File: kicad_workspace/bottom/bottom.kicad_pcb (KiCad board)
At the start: 4 copper layers, 76.8 x 84 mm, 76 parts, among them J1 691103110002, J2 BackupPad, J4 RPI_POWER_CONN, J5 UART_HEADER, J6 BackupPad, J7 Conn_01x05_Pin, M1 N20_MOTOR_EXTENDED_SHAFT, M2 N20_MOTOR_EXTENDED_SHAFT, U1 DRV8833PWP, U12 ACS712-5A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

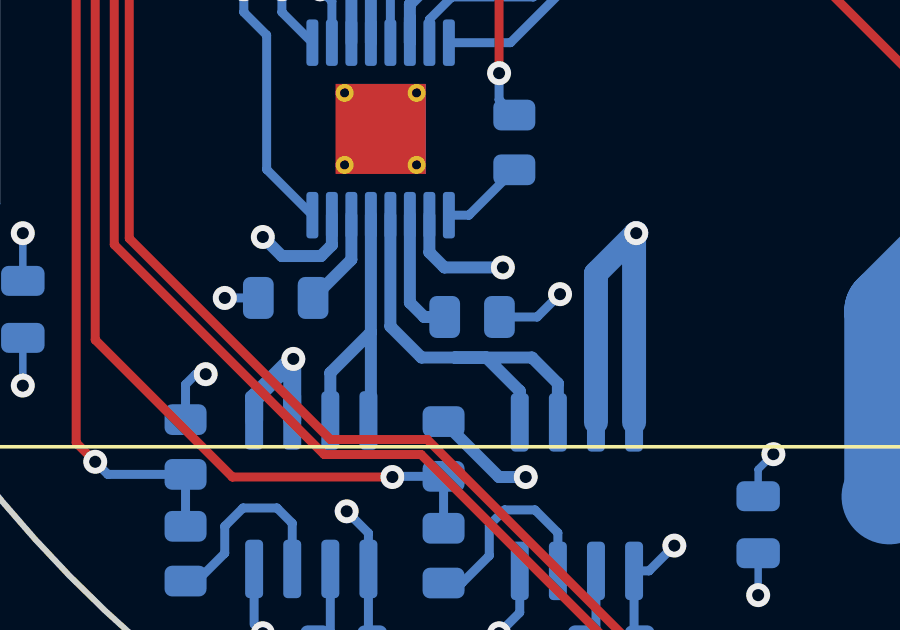
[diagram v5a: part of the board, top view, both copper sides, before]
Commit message: add additional vias for motor pins
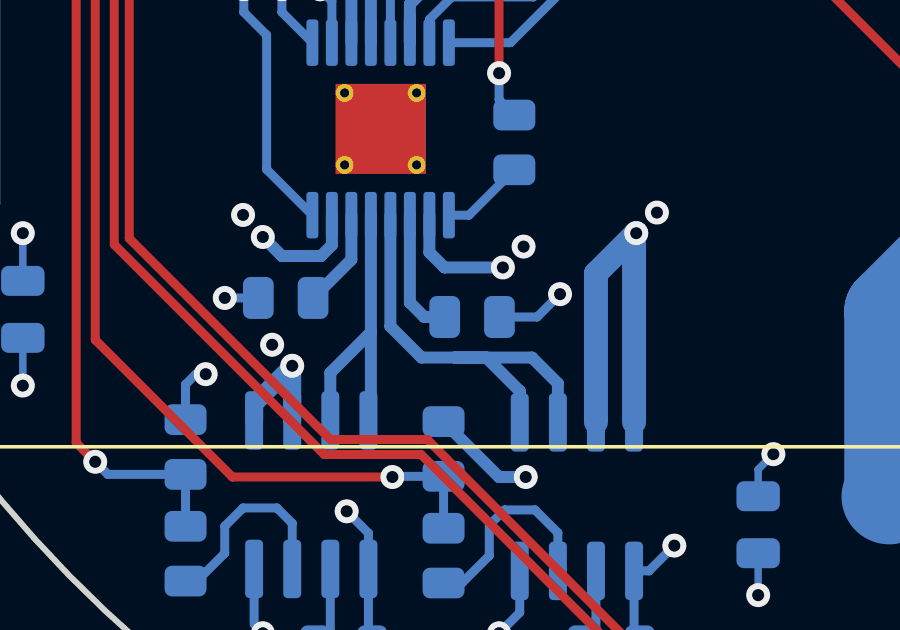
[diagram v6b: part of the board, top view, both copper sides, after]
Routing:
- net /MOTOR_B-: track 53.5 -> 55.6 mm, vias 2 -> 3
- net IP_MOTOR_B+: track 60.7 -> 62.7 mm, vias 2 -> 3
- net IP_MOTOR_A+: vias 2 -> 3
- net /MOTOR_A-: vias 2 -> 3
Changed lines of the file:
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@@
     (fp_arc (start -4.277996 -4.277996) (mid -5.350166 -3.264983) (end -6.75 -2.8)
       (stroke (width 0.12) (type solid)) (layer "B.SilkS"))
-    (fp_arc (start 4.277996 4.277996) (mid 5.350166 3.264983) (end 6.75 2.8)
+    (fp_arc (start 4.277996 4.277996) (mid 5.350166 3.264984) (end 6.75 2.8)
       (stroke (width 0.12) (type solid)) (layer "B.SilkS"))
     (fp_arc (start 5.988332 0.861605) (mid 0 6.049999) (end -5.988332 0.861605)
@@
   (segment (start 58.674 63.754) (end 58.674 65.532) (width 1) (layer "F.Cu") (net 5))
   (segment (start 55.8 63) (end 57.92 63) (width 1) (layer "F.Cu") (net 5))
+  (via (at 49.585355 77.290955) (size 0.8) (drill 0.4) (layers "F.Cu" "B.Cu") (net 5))
   (via (at 48.895 77.978) (size 0.8) (drill 0.4) (layers "F.Cu" "B.Cu") (net 5))
   (via (at 58.674 65.532) (size 0.8) (drill 0.4) (layers "F.Cu" "B.Cu") (net 5))
-  (segment (start 49.60175 77.270853) (end 50.886618 75.985985) (width 1.5) (layer "In2.Cu") (net 5))
+  (segment (start 50.886618 75.985985) (end 50.886618 73.319382) (width 1.5) (layer "In2.Cu") (net 5))
+  (segment (start 49.585355 77.287248) (end 50.886618 75.985985) (width 1.5) (layer "In2.Cu") (net 5))
   (segment (start 50.886618 73.319382) (end 58.674 65.532) (width 1.5) (layer "In2.Cu") (net 5))
+  (segment (start 49.585355 77.290955) (end 49.585355 77.287248) (width 1.5) (layer "In2.Cu") (net 5))
   (segment (start 49.515132 77.357868) (end 48.895 77.978) (width 1.5) (layer "In2.Cu") (net 5))
-  (segment (start 50.886618 75.985985) (end 50.886618 73.319382) (width 1.5) (layer "In2.Cu") (net 5))
   (segment (start 48.895 77.978) (end 48.895 77.926326) (width 0.8) (layer "In2.Cu") (net 5))
+  (segment (start 49.585355 77.287248) (end 49.60175 77.270853) (width 1.5) (layer "In2.Cu") (net 5))
   (segment (start 48.823 78.05) (end 48.895 77.978) (width 0.8) (layer "B.Cu") (net 5))
   (segment (start 47.553 79.32) (end 47.553 84.285) (width 0.8) (layer "B.Cu") (net 5))
@@
   (segment (start 55.8 65) (end 53.425875 65) (width 1) (layer "F.Cu") (net 97))
   (via (at 44.45 79.121) (size 0.8) (drill 0.4) (layers "F.Cu" "B.Cu") (net 97))
+  (via (at 45.140488 78.425612) (size 0.8) (drill 0.4) (layers "F.Cu" "B.Cu") (net 97))
   (via (at 53.408501 64.982626) (size 0.8) (drill 0.4) (layers "F.Cu" "B.Cu") (net 97))
-  (segment (start 44.45 79.121) (end 47.244 76.327) (width 1.5) (layer "In2.Cu") (net 97))
+  (segment (start 45.140488 78.425612) (end 45.140488 78.430512) (width 1.5) (layer "In2.Cu") (net 97))
   (segment (start 47.244 71.147127) (end 49.289564 69.101564) (width 1.5) (layer "In2.Cu") (net 97))
+  (segment (start 45.145388 78.425612) (end 47.244 76.327) (width 1.5) (layer "In2.Cu") (net 97))
+  (segment (start 47.244 76.327) (end 47.244 71.147127) (width 1.5) (layer "In2.Cu") (net 97))
+  (segment (start 45.140488 78.425612) (end 45.145388 78.425612) (width 1.5) (layer "In2.Cu") (net 97))
   (segment (start 49.289564 69.101564) (end 53.408501 64.982626) (width 1.5) (layer "In2.Cu") (net 97))
+  (segment (start 45.140488 78.430512) (end 44.45 79.121) (width 1.5) (layer "In2.Cu") (net 97))
   (segment (start 47.779128 70.612) (end 49.289564 69.101564) (width 1.5) (layer "In2.Cu") (net 97))
-  (segment (start 47.244 76.327) (end 47.244 71.147127) (width 1.5) (layer "In2.Cu") (net 97))
   (segment (start 42.5025 79.121) (end 42 78.6185) (width 0.4) (layer "B.Cu") (net 97))
   (segment (start 42 78.6185) (end 42 77.378) (width 0.4) (layer "B.Cu") (net 97))
@@
   (segment (start 66.294 58.674) (end 64.62 57) (width 1) (layer "F.Cu") (net 98))
   (segment (start 66.294 61.468) (end 66.294 58.674) (width 1) (layer "F.Cu") (net 98))
+  (via (at 35.789368 77.370148) (size 0.8) (drill 0.4) (layers "F.Cu" "B.Cu") (net 98))
   (via (at 66.548 61.722) (size 0.8) (drill 0.4) (layers "F.Cu" "B.Cu") (net 98))
   (via (at 36.449 78.105) (size 0.8) (drill 0.4) (layers "F.Cu" "B.Cu") (net 98))
+  (segment (start 35.714148 77.370148) (end 36.449 78.105) (width 1.5) (layer "In2.Cu") (net 98))
   (segment (start 50.135101 82.452899) (end 40.796899 82.452899) (width 1.5) (layer "In2.Cu") (net 98))
   (segment (start 66.548 61.722) (end 67.564 62.738) (width 1.5) (layer "In2.Cu") (net 98))
   (segment (start 67.564 65.024) (end 50.135101 82.452899) (width 1.5) (layer "In2.Cu") (net 98))
+  (segment (start 35.789368 77.370148) (end 35.714148 77.370148) (width 1.5) (layer "In2.Cu") (net 98))
+  (segment (start 35.789368 77.445368) (end 35.789368 77.370148) (width 1.5) (layer "In2.Cu") (net 98))
   (segment (start 67.564 62.738) (end 67.564 65.024) (width 1.5) (layer "In2.Cu") (net 98))
-  (segment (start 40.796899 82.452899) (end 36.449 78.105) (width 1.5) (layer "In2.Cu") (net 98))
+  (segment (start 40.796899 82.452899) (end 35.789368 77.445368) (width 1.5) (layer "In2.Cu") (net 98))
   (segment (start 38.75 78.3755) (end 38.3855 78.74) (width 0.4) (layer "B.Cu") (net 98))
   (segment (start 38.3855 78.74) (end 37.084 78.74) (width 0.4) (layer "B.Cu") (net 98))
@@
   (segment (start 64.2 55) (end 64.825056 55) (width 1) (layer "F.Cu") (net 102))
   (segment (start 68.453 58.801) (end 64.652 55) (width 1) (layer "F.Cu") (net 102))
-  (via (at 37.465 82.169) (size 0.8) (drill 0.4) (layers "F.Cu" "B.Cu") (net 102))
+  (via (at 37.428125 82.398765) (size 0.8) (drill 0.4) (layers "F.Cu" "B.Cu") (net 102))
   (via (at 68.453 58.801) (size 0.8) (drill 0.4) (layers "F.Cu" "B.Cu") (net 102))
-  (segment (start 39.20533 84.363798) (end 37.465 82.623468) (width 1.5) (layer "In2.Cu") (net 102))
-  (segment (start 70.612 65.278) (end 51.526202 84.363798) (width 1.5) (layer "In2.Cu") (net 102))
-  (segment (start 51.526202 84.363798) (end 39.20533 84.363798) (width 1.5) (layer "In2.Cu") (net 102))
-  (segment (start 37.465 82.623468) (end 37.465 82.169) (width 1.5) (layer "In2.Cu") (net 102))
-  (segment (start 68.453 58.801) (end 70.612 60.96) (width 1.5) (layer "In2.Cu") (net 102))
-  (segment (start 70.612 60.96) (end 70.612 65.278) (width 1.5) (layer "In2.Cu") (net 102))
-  (segment (start 36.158125 83.475875) (end 37.465 82.169) (width 0.6) (layer "B.Cu") (net 102))
-  (segment (start 37.428125 84.22) (end 37.428125 82.205875) (width 0.6) (layer "B.Cu") (net 102))
-  (segment (start 37.428125 82.205875) (end 37.465 82.169) (width 0.6) (layer "B.Cu") (net 102))
-  (segment (start 36.158125 84.22) (end 36.158125 83.475875) (width 0.6) (layer "B.Cu") (net 102))
+  (via (at 36.758752 81.696888) (size 0.8) (drill 0.4) (layers "F.Cu" "B.Cu") (net 102))
+  (segment (start 51.526202 84.363798) (end 70.612 65.278) (width 1.5) (layer "In2.Cu") (net 102))
+  (segment (start 36.758752 81.696888) (end 36.758752 81.91722) (width 1.5) (layer "In2.Cu") (net 102))
+  (segment (start 70.612 65.278) (end 70.612 60.96) (width 1.5) (layer "In2.Cu") (net 102))
+  (segment (start 36.660159 81.818627) (end 37.872766 83.031234) (width 1.5) (layer "In2.Cu") (net 102))
+  (segment (start 39.20533 84.363798) (end 51.526202 84.363798) (width 1.5) (layer "In2.Cu") (net 102))
+  (segment (start 37.872766 83.031234) (end 39.20533 84.363798) (width 1.5) (layer "In2.Cu") (net 102))
+  (segment (start 70.612 60.96) (end 68.453 58.801) (width 1.5) (layer "In2.Cu") (net 102))
+  (segment (start 36.758752 81.91722) (end 37.872766 83.031234) (width 1.5) (layer "In2.Cu") (net 102))
+  (segment (start 36.158125 83.668765) (end 36.158125 84.22) (width 0.6) (layer "B.Cu") (net 102))
+  (segment (start 37.428125 82.398765) (end 37.428125 84.22) (width 0.6) (layer "B.Cu") (net 102))
+  (segment (start 37.428125 82.398765) (end 36.158125 83.668765) (width 0.6) (layer "B.Cu") (net 102))
   (segment (start 42.65 77.378) (end 43.319 77.378) (width 0.3) (layer "B.Cu") (net 103))
   (segment (start 43.319 77.378) (end 44.831 75.866) (width 0.3) (layer "B.Cu") (net 103))

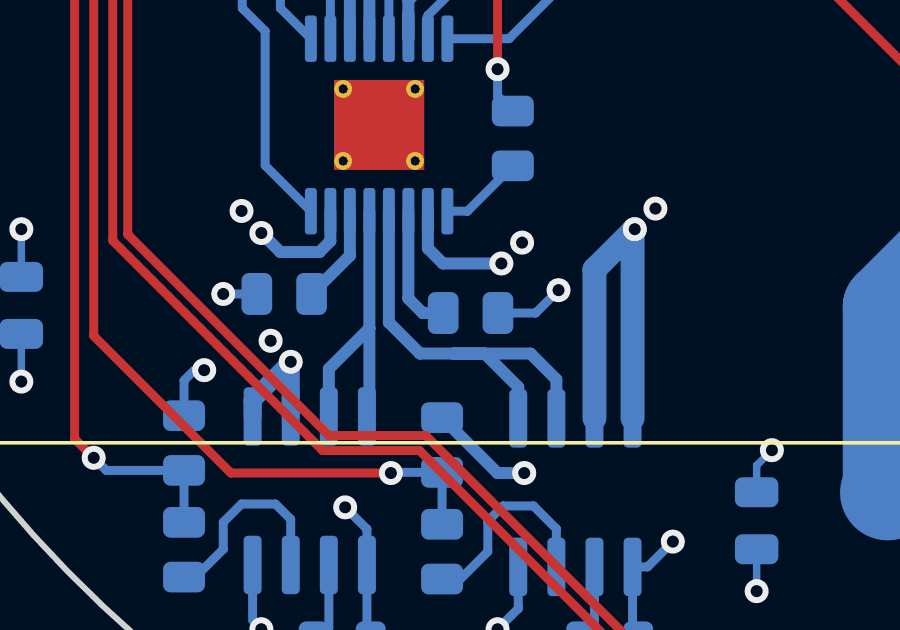
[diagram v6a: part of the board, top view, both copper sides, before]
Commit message: fix traces
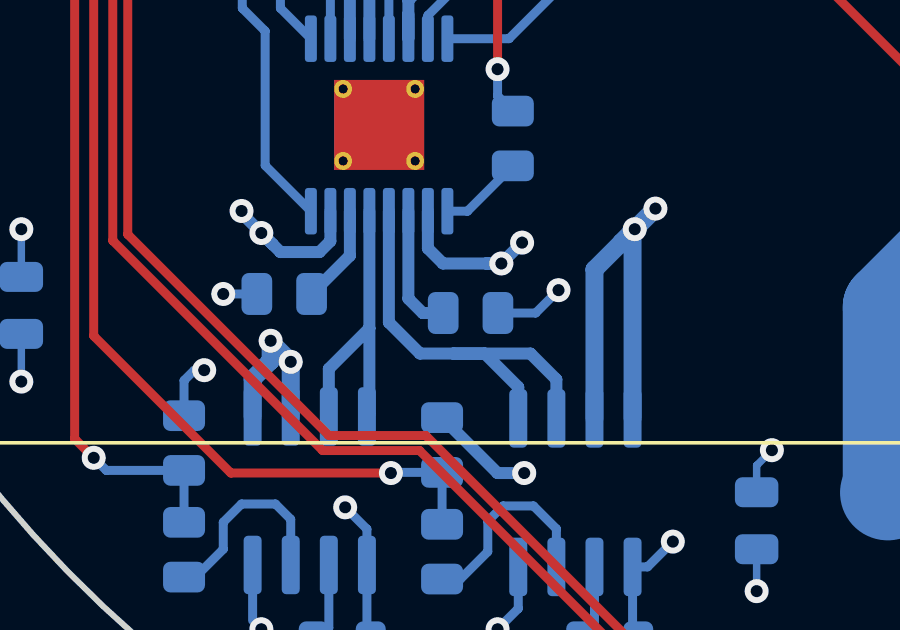
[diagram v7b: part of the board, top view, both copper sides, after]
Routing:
- net IP_MOTOR_A+: track 34.6 -> 36.2 mm
- net /MOTOR_B-: track 55.6 -> 57.2 mm
- net /MOTOR_A-: track 26.3 -> 27.8 mm
- net IP_MOTOR_B+: track 62.7 -> 64.1 mm
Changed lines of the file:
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@@
     (fp_arc (start -4.277996 -4.277996) (mid -5.350166 -3.264983) (end -6.75 -2.8)
       (stroke (width 0.12) (type solid)) (layer "B.SilkS"))
-    (fp_arc (start 4.277996 4.277996) (mid 5.350166 3.264984) (end 6.75 2.8)
+    (fp_arc (start 4.277996 4.277996) (mid 5.350166 3.264983) (end 6.75 2.8)
       (stroke (width 0.12) (type solid)) (layer "B.SilkS"))
     (fp_arc (start 5.988332 0.861605) (mid 0 6.049999) (end -5.988332 0.861605)
@@
   (segment (start 48.895 77.978) (end 48.895 77.926326) (width 0.8) (layer "In2.Cu") (net 5))
   (segment (start 49.585355 77.287248) (end 49.60175 77.270853) (width 1.5) (layer "In2.Cu") (net 5))
-  (segment (start 48.823 78.05) (end 48.895 77.978) (width 0.8) (layer "B.Cu") (net 5))
-  (segment (start 47.553 79.32) (end 47.553 84.285) (width 0.8) (layer "B.Cu") (net 5))
-  (segment (start 48.895 77.978) (end 47.553 79.32) (width 0.8) (layer "B.Cu") (net 5))
-  (segment (start 48.823 84.285) (end 48.823 78.05) (width 0.8) (layer "B.Cu") (net 5))
+  (segment (start 49.582045 77.290955) (end 49.585355 77.290955) (width 0.6) (layer "B.Cu") (net 5))
+  (segment (start 48.823 78.05) (end 48.895 77.978) (width 0.6) (layer "B.Cu") (net 5))
+  (segment (start 47.553 79.32) (end 47.553 84.285) (width 0.6) (layer "B.Cu") (net 5))
+  (segment (start 48.4505 78.4225) (end 47.553 79.32) (width 0.6) (layer "B.Cu") (net 5))
+  (segment (start 48.4505 78.4225) (end 49.582045 77.290955) (width 0.6) (layer "B.Cu") (net 5))
+  (segment (start 48.895 77.978) (end 48.4505 78.4225) (width 0.6) (layer "B.Cu") (net 5))
+  (segment (start 48.823 84.285) (end 48.823 78.05) (width 0.6) (layer "B.Cu") (net 5))
   (segment (start 62.746 63) (end 62.738 62.992) (width 0.25) (layer "F.Cu") (net 6))
   (segment (start 64.2 63) (end 62.746 63) (width 1) (layer "F.Cu") (net 6))
@@
   (segment (start 47.779128 70.612) (end 49.289564 69.101564) (width 1.5) (layer "In2.Cu") (net 97))
   (segment (start 42.5025 79.121) (end 42 78.6185) (width 0.4) (layer "B.Cu") (net 97))
+  (segment (start 44.45 79.121) (end 43.942 79.121) (width 0.4) (layer "B.Cu") (net 97))
   (segment (start 42 78.6185) (end 42 77.378) (width 0.4) (layer "B.Cu") (net 97))
-  (segment (start 44.45 79.121) (end 42.5025 79.121) (width 0.4) (layer "B.Cu") (net 97))
+  (segment (start 43.942 79.121) (end 44.4451 79.121) (width 0.4) (layer "B.Cu") (net 97))
+  (segment (start 43.942 79.121) (end 42.5025 79.121) (width 0.4) (layer "B.Cu") (net 97))
+  (segment (start 44.4451 79.121) (end 45.140488 78.425612) (width 0.4) (layer "B.Cu") (net 97))
   (segment (start 66.548 61.722) (end 66.294 61.468) (width 1) (layer "F.Cu") (net 98))
   (segment (start 64.62 57) (end 64.2 57) (width 1) (layer "F.Cu") (net 98))
@@
   (segment (start 40.796899 82.452899) (end 35.789368 77.445368) (width 1.5) (layer "In2.Cu") (net 98))
   (segment (start 38.75 78.3755) (end 38.3855 78.74) (width 0.4) (layer "B.Cu") (net 98))
+  (segment (start 37.084 78.74) (end 36.83 78.486) (width 0.4) (layer "B.Cu") (net 98))
+  (segment (start 36.83 78.486) (end 36.449 78.105) (width 0.4) (layer "B.Cu") (net 98))
+  (segment (start 36.83 78.486) (end 35.789368 77.445368) (width 0.4) (layer "B.Cu") (net 98))
+  (segment (start 35.789368 77.445368) (end 35.789368 77.370148) (width 0.4) (layer "B.Cu") (net 98))
   (segment (start 38.3855 78.74) (end 37.084 78.74) (width 0.4) (layer "B.Cu") (net 98))
   (segment (start 38.75 77.378) (end 38.75 78.3755) (width 0.4) (layer "B.Cu") (net 98))
-  (segment (start 37.084 78.74) (end 36.449 78.105) (width 0.4) (layer "B.Cu") (net 98))
   (segment (start 46.228 43.942) (end 49.53 43.942) (width 0.3) (layer "F.Cu") (net 99))
   (via (at 46.228 43.942) (size 0.8) (drill 0.4) (layers "F.Cu" "B.Cu") (net 99))
@@
   (segment (start 70.612 60.96) (end 68.453 58.801) (width 1.5) (layer "In2.Cu") (net 102))
   (segment (start 36.758752 81.91722) (end 37.872766 83.031234) (width 1.5) (layer "In2.Cu") (net 102))
-  (segment (start 36.158125 83.668765) (end 36.158125 84.22) (width 0.6) (layer "B.Cu") (net 102))
+  (segment (start 36.758752 81.729392) (end 37.428125 82.398765) (width 0.6) (layer "B.Cu") (net 102))
+  (segment (start 36.758752 82.367248) (end 36.758752 81.696888) (width 0.6) (layer "B.Cu") (net 102))
   (segment (start 37.428125 82.398765) (end 37.428125 84.22) (width 0.6) (layer "B.Cu") (net 102))
-  (segment (start 37.428125 82.398765) (end 36.158125 83.668765) (width 0.6) (layer "B.Cu") (net 102))
+  (segment (start 36.158125 82.967875) (end 36.758752 82.367248) (width 0.6) (layer "B.Cu") (net 102))
+  (segment (start 36.158125 84.22) (end 36.158125 82.967875) (width 0.6) (layer "B.Cu") (net 102))
+  (segment (start 36.758752 81.696888) (end 36.758752 81.729392) (width 0.6) (layer "B.Cu") (net 102))
   (segment (start 42.65 77.378) (end 43.319 77.378) (width 0.3) (layer "B.Cu") (net 103))
   (segment (start 43.319 77.378) (end 44.831 75.866) (width 0.3) (layer "B.Cu") (net 103))
